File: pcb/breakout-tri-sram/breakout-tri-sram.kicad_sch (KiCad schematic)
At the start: 16 parts, among them J101 FX18-120P-0.8SV20, J102 FX18-120S-0.8SV20, U101 IS61WV102416DBLL-10TLI, U102 IS61WV102416DBLL-10TLI, U103 IS61WV102416DBLL-10TLI

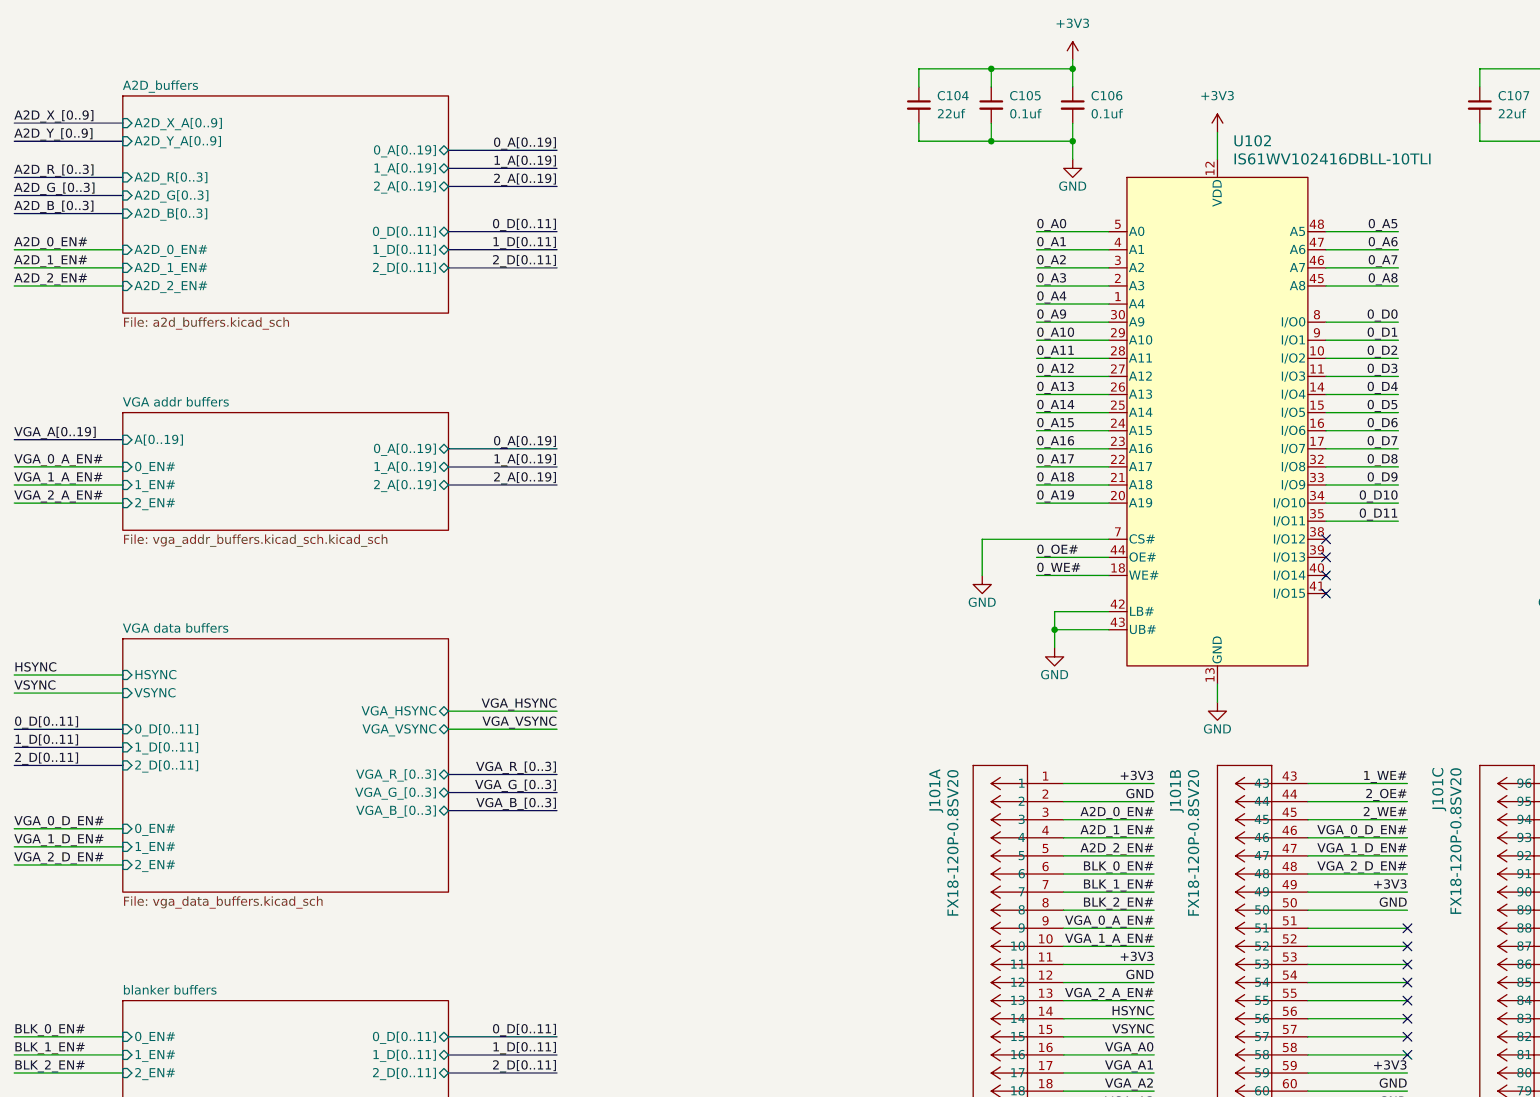
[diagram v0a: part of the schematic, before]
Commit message: [pci][pci-sram] move to latched buffers
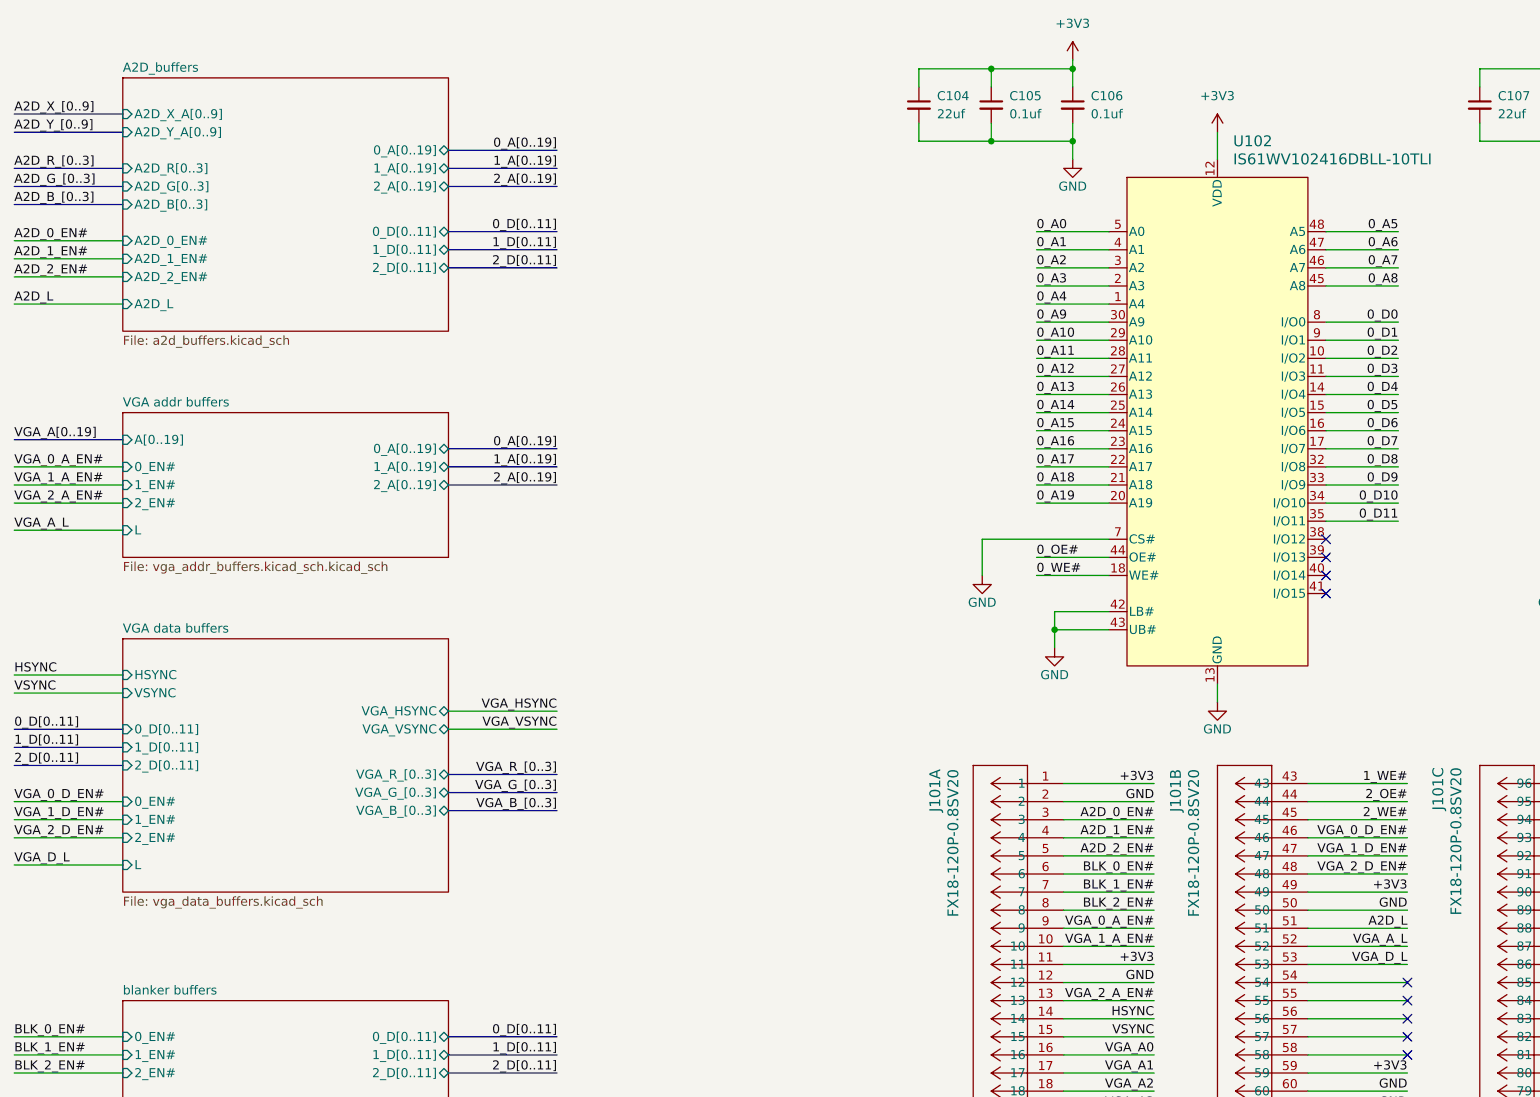
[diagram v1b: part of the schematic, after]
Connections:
- net A2D_L: now reaches J101.51
- net VGA_A_L: now reaches J101.52
- net VGA_D_L: now reaches J101.53
- no-connect marks 104 -> 101
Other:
- sheet A2D_buffers ports: added A2D_L; removed none
- sheet VGA addr buffers ports: added L; removed none
- sheet VGA data buffers ports: added L; removed none
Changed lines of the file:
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@@
 	)
 	(no_connect
-		(at 242.57 146.05)
-	)
-	(no_connect
 		(at 347.98 143.51)
 	)
@@
 	)
 	(no_connect
-		(at 242.57 143.51)
-	)
-	(no_connect
 		(at 393.7 96.52)
 	)
@@
 	)
 	(no_connect
-		(at 242.57 148.59)
-	)
-	(no_connect
 		(at 242.57 184.15)
 	)
@@
 	(wire
 		(pts
-			(xy 46.99 134.62) (xy 62.23 134.62)
+			(xy 46.99 130.81) (xy 62.23 130.81)
 		)
 		(stroke
@@
 	(wire
 		(pts
+			(xy 46.99 87.63) (xy 62.23 87.63)
+		)
+		(stroke
+			(width 0)
+			(type default)
+		)
+	)
+	(wire
+		(pts
 			(xy 383.54 78.74) (xy 393.7 78.74)
 		)
@@
 	(bus
 		(pts
-			(xy 46.99 38.1) (xy 62.23 38.1)
+			(xy 46.99 36.83) (xy 62.23 36.83)
 		)
 		(stroke
@@
 	(bus
 		(pts
-			(xy 46.99 43.18) (xy 62.23 43.18)
+			(xy 46.99 41.91) (xy 62.23 41.91)
 		)
 		(stroke
@@
 	(wire
 		(pts
-			(xy 46.99 48.26) (xy 62.23 48.26)
+			(xy 46.99 46.99) (xy 62.23 46.99)
 		)
 		(stroke
@@
 	(bus
 		(pts
-			(xy 46.99 40.64) (xy 62.23 40.64)
+			(xy 46.99 39.37) (xy 62.23 39.37)
 		)
 		(stroke
@@
 	(wire
 		(pts
-			(xy 46.99 50.8) (xy 62.23 50.8)
+			(xy 46.99 49.53) (xy 62.23 49.53)
 		)
 		(stroke
@@
 	(wire
 		(pts
+			(xy 46.99 55.88) (xy 62.23 55.88)
+		)
+		(stroke
+			(width 0)
+			(type default)
+		)
+	)
+	(wire
+		(pts
 			(xy 368.3 109.22) (xy 368.3 111.76)
 		)
@@
 	(bus
 		(pts
-			(xy 46.99 33.02) (xy 62.23 33.02)
+			(xy 46.99 31.75) (xy 62.23 31.75)
 		)
 		(stroke
@@
 	(wire
 		(pts
-			(xy 46.99 129.54) (xy 62.23 129.54)
+			(xy 46.99 125.73) (xy 62.23 125.73)
 		)
 		(stroke
@@
 	(wire
 		(pts
-			(xy 46.99 132.08) (xy 62.23 132.08)
+			(xy 46.99 128.27) (xy 62.23 128.27)
 		)
 		(stroke
@@
 	(wire
 		(pts
-			(xy 46.99 53.34) (xy 62.23 53.34)
+			(xy 46.99 52.07) (xy 62.23 52.07)
 		)
 		(stroke
@@
 	(wire
 		(pts
+			(xy 46.99 134.62) (xy 62.23 134.62)
+		)
+		(stroke
+			(width 0)
+			(type default)
+		)
+	)
+	(wire
+		(pts
 			(xy 347.98 179.07) (xy 358.14 179.07)
 		)
@@
 	(bus
 		(pts
-			(xy 46.99 30.48) (xy 62.23 30.48)
+			(xy 46.99 29.21) (xy 62.23 29.21)
 		)
 		(stroke
@@
 	)
 	(label "A2D_2_EN#"
-		(at 46.99 53.34 0)
+		(at 46.99 52.07 0)
 		(fields_autoplaced yes)
 		(effects
@@
 	)
 	(label "A2D_G_[0..3]"
-		(at 46.99 40.64 0)
+		(at 46.99 39.37 0)
 		(fields_autoplaced yes)
 		(effects
@@
 	)
 	(label "A2D_B_[0..3]"
-		(at 46.99 43.18 0)
+		(at 46.99 41.91 0)
 		(fields_autoplaced yes)
 		(effects
@@
 		)
 	)
+	(label "VGA_D_L"
+		(at 242.57 148.59 180)
+		(fields_autoplaced yes)
+		(effects
+			(font
+				(size 1.27 1.27)
+			)
+			(justify right bottom)
+		)
+	)
 	(label "0_OE#"
 		(at 190.5 91.44 0)
@@
 	)
 	(label "A2D_1_EN#"
-		(at 46.99 50.8 0)
+		(at 46.99 49.53 0)
 		(fields_autoplaced yes)
 		(effects
@@
 		)
 	)
+	(label "VGA_A_L"
+		(at 242.57 146.05 180)
+		(fields_autoplaced yes)
+		(effects
+			(font
+				(size 1.27 1.27)
+			)
+			(justify right bottom)
+		)
+	)
 	(label "+3V3"
 		(at 384.81 161.29 0)
@@
 		)
 	)
+	(label "VGA_D_L"
+		(at 46.99 134.62 0)
+		(fields_autoplaced yes)
+		(effects
+			(font
+				(size 1.27 1.27)
+			)
+			(justify left bottom)
+		)
+	)
 	(label "0_WE#"
 		(at 207.01 224.79 180)
@@
 	)
 	(label "A2D_R_[0..3]"
-		(at 46.99 38.1 0)
+		(at 46.99 36.83 0)
 		(fields_autoplaced yes)
 		(effects
@@
 	)
 	(label "A2D_0_EN#"
-		(at 46.99 48.26 0)
+		(at 46.99 46.99 0)
 		(fields_autoplaced yes)
 		(effects
@@
 	)
 	(label "VGA_2_D_EN#"
-		(at 46.99 134.62 0)
+		(at 46.99 130.81 0)
 		(fields_autoplaced yes)
 		(effects
@@
 	)
 	(label "VGA_1_D_EN#"
-		(at 46.99 132.08 0)
+		(at 46.99 128.27 0)
 		(fields_autoplaced yes)
 		(effects
@@
 	)
 	(label "A2D_Y_[0..9]"
-		(at 46.99 33.02 0)
+		(at 46.99 31.75 0)
 		(fields_autoplaced yes)
 		(effects
@@
 		)
 	)
+	(label "A2D_L"
+		(at 242.57 143.51 180)
+		(fields_autoplaced yes)
+		(effects
+			(font
+				(size 1.27 1.27)
+			)
+			(justify right bottom)
+		)
+	)
 	(label "VGA_1_A_EN#"
 		(at 207.01 146.05 180)
@@
 		)
 	)
+	(label "A2D_L"
+		(at 46.99 55.88 0)
+		(fields_autoplaced yes)
+		(effects
+			(font
+				(size 1.27 1.27)
+			)
+			(justify left bottom)
+		)
+	)
 	(label "A2D_X_[0..9]"
-		(at 46.99 30.48 0)
+		(at 46.99 29.21 0)
 		(fields_autoplaced yes)
 		(effects
@@
 		)
 	)
+	(label "VGA_A_L"
+		(at 46.99 87.63 0)
+		(fields_autoplaced yes)
+		(effects
+			(font
+				(size 1.27 1.27)
+			)
+			(justify left bottom)
+		)
+	)
 	(label "1_D8"
 		(at 320.04 78.74 180)
@@
 	)
 	(label "VGA_0_D_EN#"
-		(at 46.99 129.54 0)
+		(at 46.99 125.73 0)
 		(fields_autoplaced yes)
 		(effects
@@
 		)
 		(pin "1_EN#" input
-			(at 62.23 132.08 180)
+			(at 62.23 128.27 180)
 			(effects
 				(font
@@
 		)
 		(pin "2_EN#" input
-			(at 62.23 134.62 180)
+			(at 62.23 130.81 180)
 			(effects
 				(font
@@
 		)
 		(pin "0_EN#" input
-			(at 62.23 129.54 180)
+			(at 62.23 125.73 180)
 			(effects
 				(font
@@
 			)
 		)
+		(pin "L" input
+			(at 62.23 134.62 180)
+			(effects
+				(font
+					(size 1.27 1.27)
+				)
+				(justify left)
+			)
+		)
 		(instances
 			(project "breakout-tri-sram"
@@
 	)
 	(sheet
-		(at 62.23 26.67)
-		(size 45.72 30.48)
+		(at 62.23 24.13)
+		(size 45.72 35.56)
 		(fields_autoplaced yes)
 		(stroke
@@
 		)
 		(property "Sheetname" "A2D_buffers"
-			(at 62.23 25.9584 0)
+			(at 62.23 23.4184 0)
 			(effects
 				(font
@@
 		)
 		(property "Sheetfile" "a2d_buffers.kicad_sch"
-			(at 62.23 57.7346 0)
+			(at 62.23 60.2746 0)
 			(effects
 				(font
@@
 		)
 		(pin "A2D_Y_A[0..9]" input
-			(at 62.23 33.02 180)
+			(at 62.23 31.75 180)
 			(effects
 				(font
@@
 		)
 		(pin "A2D_B[0..3]" input
-			(at 62.23 43.18 180)
+			(at 62.23 41.91 180)
 			(effects
 				(font
@@
 		)
 		(pin "A2D_G[0..3]" input
-			(at 62.23 40.64 180)
+			(at 62.23 39.37 180)
 			(effects
 				(font
@@
 		)
 		(pin "A2D_R[0..3]" input
-			(at 62.23 38.1 180)
+			(at 62.23 36.83 180)
 			(effects
 				(font
@@
 		)
 		(pin "A2D_X_A[0..9]" input
-			(at 62.23 30.48 180)
+			(at 62.23 29.21 180)
 			(effects
 				(font
@@
 		)
 		(pin "A2D_1_EN#" input
-			(at 62.23 50.8 180)
+			(at 62.23 49.53 180)
 			(effects
 				(font
@@
 		)
 		(pin "A2D_0_EN#" input
-			(at 62.23 48.26 180)
+			(at 62.23 46.99 180)
 			(effects
 				(font
@@
 		)
 		(pin "A2D_2_EN#" input
-			(at 62.23 53.34 180)
+			(at 62.23 52.07 180)
 			(effects
 				(font
@@
 			)
 		)
+		(pin "A2D_L" input
+			(at 62.23 55.88 180)
+			(effects
+				(font
+					(size 1.27 1.27)
+				)
+				(justify left)
+			)
+		)
 		(instances
 			(project "breakout-tri-sram"
@@
 	(sheet
 		(at 62.23 71.12)
-		(size 45.72 16.51)
+		(size 45.72 20.32)
 		(fields_autoplaced yes)
 		(stroke
@@
 		)
 		(property "Sheetfile" "vga_addr_buffers.kicad_sch.kicad_sch"
-			(at 62.23 88.2146 0)
+			(at 62.23 92.0246 0)
 			(effects
 				(font
@@
 			)
 		)
+		(pin "L" input
+			(at 62.23 87.63 180)
+			(effects
+				(font
+					(size 1.27 1.27)
+				)
+				(justify left)
+			)
+		)

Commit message: [pcb][tri-sram] tri-sram complete
squashed big-bus branch
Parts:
- added C101: 0.1uf, Capacitor_SMD:C_0402_1005Metric, symbol Device:C_Small
- added PM103: Conn_02x06_Top_Bottom, custom:PMOD_12p_Horizontal, symbol Connector_Generic:Conn_02x06_Top_Bottom
- added U101: 74LS573, Package_SO:SSOP-20_4.4x6.5mm_P0.65mm, symbol 74xx:74LS573
- renumbered C104 to C102, C105 to C103, C106 to C104, C107 to C105, C108 to C106, C109 to C107, C101 to C108, C102 to C109, C103 to C110, U101 to U104
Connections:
- net A2D_R_2 is gone; now on net A2D_X6: J102.37
- net A2D_R_3 is gone; now on net A2D_X5: J102.38
- net +3V3: now also C101.1, PM103.12 (Pin_12), PM103.6 (Pin_6), U101.20 (VCC)
- net 0_OE#: now also J101.27, U101.6 (D4); no longer J101.38, U102.44 (OE#)
- net 0_WE#: now also J101.30, U101.9 (D7); no longer J101.41, U102.18 (WE#)
- net 1_OE#: now also J101.26, U101.5 (D3); no longer J101.42, U103.44 (OE#)
- net 1_WE#: now also J101.29, U101.8 (D6); no longer J101.43, U103.18 (WE#)
- net 2_OE#: now also J101.25, U101.4 (D2); no longer J101.44, U104.44 (OE#)
- net 2_WE#: now also J101.28, U101.7 (D5); no longer J101.45, U104.18 (WE#)
- net A2D_0_EN#: now also J101.32; no longer J101.3
- net A2D_1_EN#: now also J101.34; no longer J101.4
- net A2D_2_EN#: now also J101.33; no longer J101.5
- net A2D_L: now also J101.55; no longer J101.51
- net BLK_0_EN#: now also J101.18; no longer J101.6
- net BLK_1_EN#: now also J101.16; no longer J101.7
- net BLK_2_EN#: now also J101.14; no longer J101.8
- net GND: now also C101.2, PM103.11 (Pin_11), PM103.5 (Pin_5), U101.1 (OE), U101.10 (GND)
- net HSYNC: now also J101.23, U101.2 (D0); no longer J101.14
- net VGA_0_A_EN#: now also J101.43; no longer J101.9
- net VGA_0_D_EN#: now also J101.19; no longer J101.46
- net VGA_1_A_EN#: now also J101.42; no longer J101.10
- net VGA_1_D_EN#: now also J101.17; no longer J101.47
- net VGA_2_A_EN#: now also J101.41; no longer J101.13
- net VGA_2_D_EN#: now also J101.15; no longer J101.48
- net VGA_A0: now also J101.54; no longer J101.16
- net VGA_A1: now also J101.38; no longer J101.17
- net VGA_A10: now also J101.7; no longer J101.28
- net VGA_A11: now also J101.6; no longer J101.29
- net VGA_A12: now also J101.5; no longer J101.30
- net VGA_A13: now also J101.4; no longer J101.31
- net VGA_A14: now also J101.3; no longer J101.32
- net VGA_A15: now also J101.47; no longer J101.33
- net VGA_A16: now also J101.48; no longer J101.34
- net VGA_A17: now also J101.51; no longer J101.35
- net VGA_A18: now also J101.52; no longer J101.36
- net VGA_A19: now also J101.53; no longer J101.37
- net VGA_A2: now also J101.37; no longer J101.18
- net VGA_A3: now also J101.36; no longer J101.19
- net VGA_A4: now also J101.35; no longer J101.20
- net VGA_A5: now also J101.45; no longer J101.23
- net VGA_A6: now also J101.46; no longer J101.24
- net VGA_A7: now also J101.10; no longer J101.25
- net VGA_A8: now also J101.9; no longer J101.26
- net VGA_A9: now also J101.8; no longer J101.27
- net VGA_A_L: now also J101.44; no longer J101.52
- net VGA_D_L: now also J101.13; no longer J101.53
- net VGA_HSYNC: now also U101.19 (Q0)
- net VGA_VSYNC: now also U101.18 (Q1)
- net VSYNC: now also J101.24, U101.3 (D1); no longer J101.15
- net LK_01: now reaches J101.111
- net LK_01: now also PM103.1 (Pin_1)
- net LK_05: now reaches J101.112
- net LK_05: now also PM103.7 (Pin_7)
- net LK_02: now reaches J101.113
- net LK_02: now also PM103.2 (Pin_2)
- net LK_06: now reaches J101.114
- net LK_06: now also PM103.8 (Pin_8)
- net LK_03: now reaches J101.115
- net LK_03: now also PM103.3 (Pin_3)
- net LK_07: now reaches J101.116
- net LK_07: now also PM103.9 (Pin_9)
- net LK_04: now reaches J101.117
- net LK_04: now also PM103.4 (Pin_4)
- net LK_08: now reaches J101.118
- net LK_08: now also PM103.10 (Pin_10)
- net A2D_X6: now reaches J101.97
- net A2D_X5: now reaches J101.98
- net A2D_B_0 renamed A2D_B0
- net A2D_B_1 renamed A2D_B1
- net A2D_B_2 renamed A2D_B2
- net A2D_B_3 renamed A2D_B3
- net A2D_G_0 renamed A2D_X0
- net A2D_G_1 renamed A2D_Y9
- net A2D_G_2 renamed A2D_Y8
- net A2D_G_3 renamed A2D_Y7
- net A2D_R_0 renamed A2D_Y6
- net A2D_R_1 renamed A2D_Y5
- net A2D_X_0 renamed A2D_X7
- net A2D_X_1 renamed A2D_X8
- net A2D_X_2 renamed A2D_X9
- net A2D_X_3 renamed A2D_Y0
- net A2D_X_4 renamed A2D_Y1
- net A2D_X_5 renamed A2D_Y2
- net A2D_X_6 renamed A2D_Y3
- net A2D_X_7 renamed A2D_Y4
- net A2D_X_8 renamed A2D_G0
- net A2D_X_9 renamed A2D_G1
- net A2D_Y_0 renamed A2D_G2
- net A2D_Y_1 renamed A2D_G3
- net A2D_Y_2 renamed A2D_R3
- net A2D_Y_3 renamed A2D_R2
- net A2D_Y_4 renamed A2D_R1
- net A2D_Y_5 renamed A2D_R0
- net A2D_Y_6 renamed A2D_X1
- net A2D_Y_7 renamed A2D_X2
- net A2D_Y_8 renamed A2D_X3
- net A2D_Y_9 renamed A2D_X4
- net VGA_B_0 renamed VGA_B0
- net VGA_B_1 renamed VGA_B1
- net VGA_B_2 renamed VGA_B2
- net VGA_B_3 renamed VGA_B3
- net VGA_G_0 renamed VGA_G0
- net VGA_G_1 renamed VGA_G1
- net VGA_G_2 renamed VGA_G2
- net VGA_G_3 renamed VGA_G3
- net VGA_R_0 renamed VGA_R0
- net VGA_R_1 renamed VGA_R1
- net VGA_R_2 renamed VGA_R2
- net VGA_R_3 renamed VGA_R3
- new net SIGL: J101.31, U101.11 (Load)
- new net S_0_OE#: U101.15 (Q4), U102.44 (OE#)
- new net S_0_WE#: U101.12 (Q7), U102.18 (WE#)
- new net S_1_OE#: U101.16 (Q3), U103.44 (OE#)
- new net S_1_WE#: U101.13 (Q6), U103.18 (WE#)
- new net S_2_OE#: U101.17 (Q2), U104.44 (OE#)
- new net S_2_WE#: U101.14 (Q5), U104.18 (WE#)
- no-connect marks 101 -> 90
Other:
- sheet A2D_buffers ports: added A2D_X[0..9], A2D_Y[0..9]; removed A2D_X_A[0..9], A2D_Y_A[0..9]
- sheet VGA addr buffers: file vga_addr_buffers.kicad_sch.kicad_sch -> vga_addr_buffers.kicad_sch
- sheet VGA data buffers ports: added VGA_B[0..3], VGA_G[0..3], VGA_R[0..3]; removed HSYNC, VGA_B_[0..3], VGA_G_[0..3], VGA_HSYNC, VGA_R_[0..3], VGA_VSYNC, VSYNC
- moved on the sheet: PM101, PM102

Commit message: [pcb][tri-sram] add part numbers
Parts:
- J101: LCSC Part # (none) -> C3650293
- J102: LCSC Part # (none) -> C598059
- U101: Digi-Key Part Number (none) -> 264-74LCX541FT(AE)CT-ND
- U102, U103, U104: Digi-Key Part Number (none) -> 706-1541-ND; LCSC Part # C1348726 -> C1348726
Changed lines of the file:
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@@
 			)
 		)
+		(property "LCSC Part #" "C3650293"
+			(at 194.31 123.19 0)
+			(effects
+				(font
+					(size 1.27 1.27)
+				)
+				(hide yes)
+			)
+		)
 		(pin "9"
 		)
@@
 			)
 		)
+		(property "LCSC Part #" "C3650293"
+			(at 228.6 123.19 0)
+			(effects
+				(font
+					(size 1.27 1.27)
+				)
+				(hide yes)
+			)
+		)
 		(pin "9"
 		)
@@
 			)
 		)
+		(property "LCSC Part #" ""
+			(at 152.4 242.57 0)
+			(effects
+				(font
+					(size 1.27 1.27)
+				)
+				(hide yes)
+			)
+		)
 		(pin "9"
 		)
@@
 			)
 		)
+		(property "LCSC Part #" "C598059"
+			(at 358.14 123.19 0)
+			(effects
+				(font
+					(size 1.27 1.27)
+				)
+				(hide yes)
+			)
+		)
 		(pin "117"
 		)
@@
 			)
 		)
+		(property "LCSC Part #" ""
+			(at 52.07 222.25 0)
+			(effects
+				(font
+					(size 1.27 1.27)
+				)
+				(hide yes)
+			)
+		)
 		(pin "9"
 		)
@@
 			)
 		)
-		(property "LCSC Part #" " C1348726"
+		(property "LCSC Part #" "C1348726"
+			(at 195.58 45.72 0)
+			(effects
+				(font
+					(size 1.27 1.27)
+				)
+				(hide yes)
+			)
+		)
+		(property "Digi-Key Part Number" "706-1541-ND"
 			(at 195.58 45.72 0)
 			(effects
@@
 			)
 		)
+		(property "LCSC Part #" "C598059"
+			(at 323.85 123.19 0)
+			(effects
+				(font
+					(size 1.27 1.27)
+				)
+				(hide yes)
+			)
+		)
 		(pin "117"
 		)
@@
 			)
 		)
-		(property "LCSC Part #" " C1348726"
+		(property "LCSC Part #" "C1348726"
+			(at 274.32 45.72 0)
+			(effects
+				(font
+					(size 1.27 1.27)
+				)
+				(hide yes)
+			)
+		)
+		(property "Digi-Key Part Number" "706-1541-ND"
 			(at 274.32 45.72 0)
 			(effects
@@
 			)
 		)
+		(property "Digi-Key Part Number" "264-74LCX541FT(AE)CT-ND"
+			(at 115.57 208.28 0)
+			(effects
+				(font
+					(size 1.27 1.27)
+				)
+				(hide yes)
+			)
+		)
 		(pin "5"
 		)
@@
 			)
 		)
+		(property "LCSC Part #" "C3650293"
+			(at 265.43 123.19 0)
+			(effects
+				(font
+					(size 1.27 1.27)
+				)
+				(hide yes)
+			)
+		)
 		(pin "9"
 		)
@@
 			)
 		)
-		(property "LCSC Part #" " C1348726"
+		(property "LCSC Part #" "C1348726"
+			(at 347.98 45.72 0)
+			(effects
+				(font
+					(size 1.27 1.27)
+				)
+				(hide yes)
+			)
+		)
+		(property "Digi-Key Part Number" "706-1541-ND"
 			(at 347.98 45.72 0)
 			(effects
@@
 			)
 		)
+		(property "LCSC Part #" "C598059"
+			(at 394.97 123.19 0)
+			(effects
+				(font
+					(size 1.27 1.27)
+				)
+				(hide yes)
+			)
+		)
 		(pin "117"
 		)
@@
 			(at 52.07 196.85 0)
 			(effects
+				(font
+					(size 1.27 1.27)
+				)
+				(hide yes)
+			)
+		)
+		(property "LCSC Part #" ""
+			(at 52.07 196.85 0)
+			(effects
